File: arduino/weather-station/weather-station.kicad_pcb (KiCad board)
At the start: 2 copper layers, 90 x 56 mm, 11 parts, among them SW1 PTS645SM43SMTR92 LFS, U1 SHT31-DIS-B2.5kS

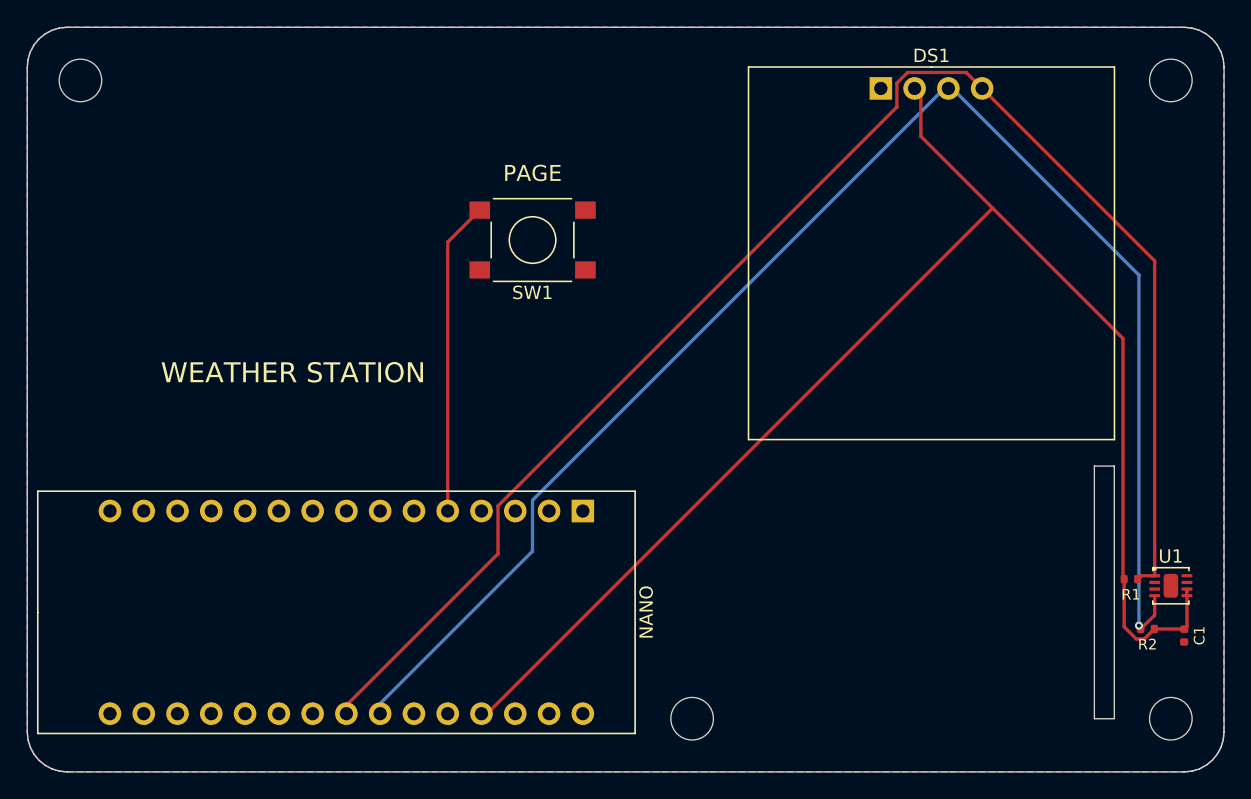
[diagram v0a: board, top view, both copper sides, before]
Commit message: registry: every board rebuilt with pcbkit main 4684674e6 - the bought part named on the board
pcbkit dc07fdfd6 writes the bought row's MPN and Manufacturer (the design's own kept as DesignMPN /
DesignManufacturer) and the build chooses parts before it places (6361ec104). Each of the 44 boards
was rebuilt (; the two P4 boards  only: their builds reroute pairs):
copper unchanged on all 44 (segments, arcs and vias counted before and after), placement kept; the
Arduino and lab boards now carry the parts the catalogue gives them. The check gains only the new
judgements: part-maker (a part bought from another maker) and part-missing on hand-fitted modules
(DS1 sockets); p4-touch-7 loses part-stale. The P4 boards keep their hole-clearance errors (a
reroute is Team 3's).

Claude-Session: https://claude.ai/code/session_01BAgp959tApA8aEg85EYgfb
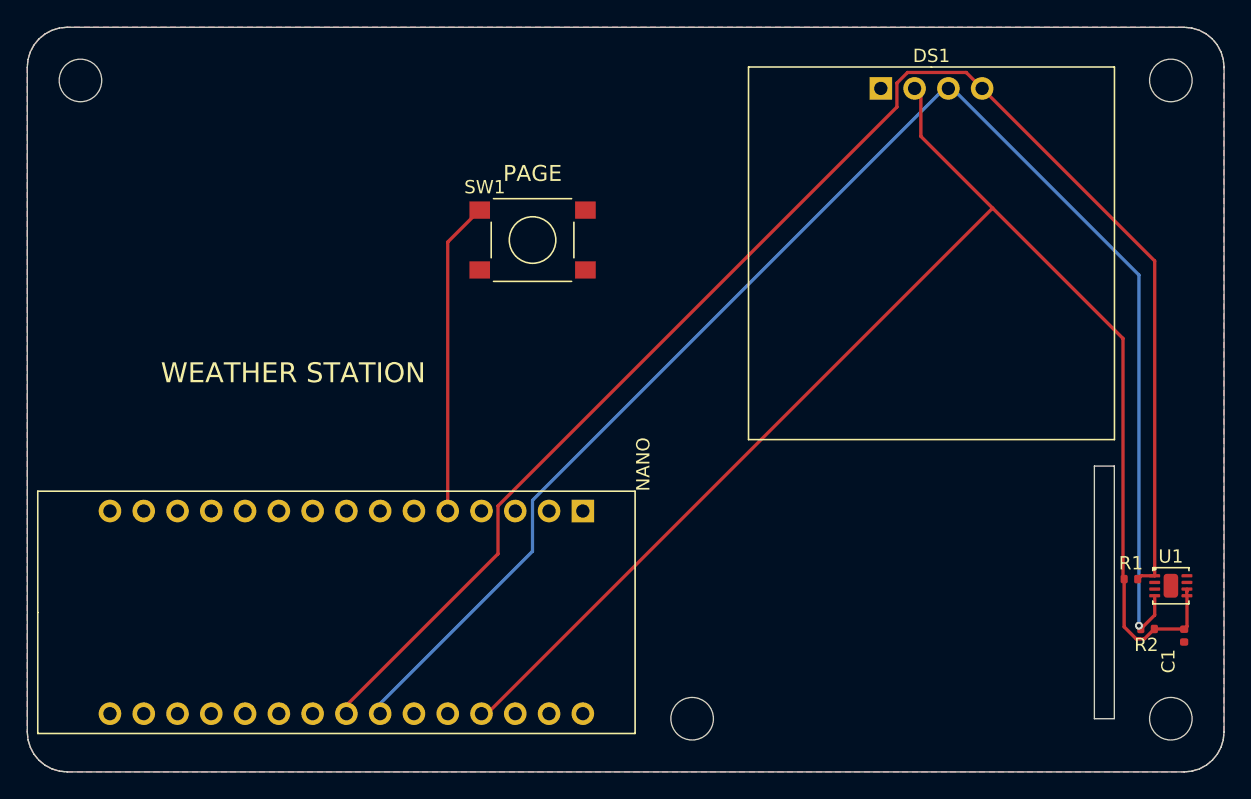
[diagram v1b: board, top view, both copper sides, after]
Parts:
- H1, H2, H3, H4: value (none) -> MountingHole_3.2mm_M3
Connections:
- SW1 pad 2: PAGE -> GND
